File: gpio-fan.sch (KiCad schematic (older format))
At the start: 26 parts, among them J1 Conn_01x05, J2 Conn_01x05, J3 Conn_01x02, J4 Conn_02x07_Odd_Even, J5 Conn_01x03, J6 Conn_01x02, J7 Conn_01x02, J8 Conn_01x02, Q1 BSS214NW, SW1 SW_DIP_x03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

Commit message: Added large via to match 3.8, minor changes
Signed-off-by: Aaron Williams <aaron.w2@gmail.com>
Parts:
- removed J5: Conn_01x03, Connector_Molex:Molex_KK-254_AE-6410-03A_1x03_P2.54mm_Vertical, symbol Connector_Generic:Conn_01x03
- added C9: 1uF, Capacitor_SMD:C_0603_1608Metric, symbol Device:C
- added J5: Conn_01x04_Male, Connector_PinHeader_2.54mm:PinHeader_1x04_P2.54mm_Vertical, symbol Connector:Conn_01x04_Male
- J2: value Conn_01x05 -> Conn_01x05 DNS
- J3: MFR - -> Samtec Inc.; MPN - -> SLM-102-01-S-S; SPN - -> SAM9931-ND; SPR - -> Digikey; SPURL - -> https://www.digikey.com/products/en?mpart=SLM-102-01-S-S&v=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
- J4: MFR - -> Adam Tech; MPN - -> BHR-14-HUA-ML; SPN - -> 2057-BHR-14-HUA-ML-ND; SPR - -> Digikey; SPURL - -> https://www.digikey.com/product-detail/en/adam-tech/BHR-14-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
- J7, J8: value Conn_01x02 -> Conn_01x02 DNS
- R1: value 4.7K -> 1K; DESC (none) -> RES SMD 1K OHM 1% 1/10W 0603; MPN RC0603FR-074K7L -> RC0603FR-071KL; SPN 311-4.70KHRCT-ND -> 311-1.00KHRCT-ND; SPURL https://www.digikey.com/product-detail/en/yageo/RC0603FR-074K7L/311-4.70KHRCT-ND/730159 -> https://www.digikey.com/product-detail/en/yageo/RC0603FR-071KL/311-1.00KHRCT-ND/729790
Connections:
- wire segments 83 -> 89

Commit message: Upgraded to revision 1.3, changed temperature sensor and accelerometer.
This now uses a combined part that should be a lot easier to solder.
The new ST part also includes a temperature sensor and it is supported
by the Arduino library.

Signed-off-by: Aaron Williams <aaron.w2@gmail.com>
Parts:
- removed U2: MXC400XXC, Aaron:MXC400XXC, symbol Aaron:MXC400XXC
- added C10: 0.22uF, Capacitor_SMD:C_0603_1608Metric, symbol Device:C
- added C11: 0.1uF, Capacitor_SMD:C_0603_1608Metric, symbol Device:C
- added C12: 10uF, Capacitor_SMD:C_0603_1608Metric, symbol Device:C
- added U2: LSM303AGRTR, Package_LGA:LGA-12_2x2mm_P0.5mm, symbol Aaron:LSM303AGRTR
- C1, C2, C3, C4, C5, C6, C7, C9, D1, D2, D3, J1, J3, J4, J5, Q1, R2, RN1, SW1, U1: DESC (none) -> -
- C8: value 1uF -> 0.1uF; DESC (none) -> -
- J6: DESC (none) -> -; SPURL https://www.digikey.com/product-detail/en/samtec-inc/SLM-10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 -> https://www.digikey.com/products/en?mpart=SLM-102-01-S-S&v=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
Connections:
- wire segments 89 -> 110
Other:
- moved on the sheet: C8, RN1, SW1

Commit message: Fixed mislabeled capacitor and other minor changes.
Signed-off-by: Aaron Williams <aaron.w2@gmail.com>
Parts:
- added C13: 0.1uF, Capacitor_SMD:C_0603_1608Metric, symbol Device:C
- U1: footprint Aaron:HWQFN-24_EP_4x4_Pitch0.5mm -> Package_DFN_QFN:Texas_S-PVQFN-N24_EP2.1x2.1mm

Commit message: Fixed J6, dimmed LEDs, and added ADC for light sensor
This also expands the board size where the switches are so that it can be
better mounted to the main board via the +5V pins near the speaker connector.

Signed-off-by: Aaron Williams <aaron.w2@gmail.com>
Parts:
- added C14: 1uF, Capacitor_SMD:C_0603_1608Metric, symbol Device:C
- added C15: 0.1uF, Capacitor_SMD:C_0603_1608Metric, symbol Device:C
- added J10: Conn_01x04 DNS, Connector_PinHeader_1.27mm:PinHeader_1x04_P1.27mm_Vertical, symbol Connector:Conn_01x04_Male
- added J9: Conn_01x04 DNS, Connector_PinHeader_2.54mm:PinHeader_1x04_P2.54mm_Vertical, symbol Connector:Conn_01x04_Male
- added R3: 4.7K, Resistor_SMD:R_0603_1608Metric, symbol Device:R
- added U3: ADS1110, Package_TO_SOT_SMD:SOT-23-6, symbol Analog_ADC:ADS1110
- J5: value Conn_01x04_Male -> Conn_01x04 DNS
- R1: value 1K -> 4.7K
- R2: value 33 -> 3.9K; DESC - -> 3.9 kOhms ±1% 0.1W, 1/10W Chip Resistor 0603 (1608 Metric) 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; MFR Yageo -> Bourns Inc.; MPN RC0603FR-0733RL -> CR0603-FX-3901ELF; SPN 311-33.0HRCT-ND -> CR0603-FX-3901ELFCT-ND; SPURL https://www.digikey.com/product-detail/en/yageo/RC0603FR-07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 -> https://www.digikey.com/en/products/detail/bourns-inc/CR060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
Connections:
- net labels added: ADC_IN, PU_OUT
- wire segments 110 -> 130

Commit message: Changed accelerometer due to unavailability
The LSM303AGRTR compass/accelerometer/etc. is out of stock in many places
so this substitutes a LSM6DSL and a LISMDLTR combination instead.

Signed-off-by: Aaron Williams <aaron.w2@gmail.com>
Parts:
- removed U2: LSM303AGRTR, Package_LGA:LGA-12_2x2mm_P0.5mm, symbol Aaron:LSM303AGRTR
- added C16, C17: 0.1uF, Capacitor_SMD:C_0603_1608Metric, symbol Device:C
- added U2: LSM6DSL, Package_LGA:LGA-14_3x2.5mm_P0.5mm_LayoutBorder3x4y, symbol Aaron:LSM6DSL
- added U4: LIS3MDLTR, digikey-footprints:VFLGA-12_2x2mm, symbol dk_Magnetic-Sensors-Linear-Compass-ICs:LIS3MDLTR
- C10: value 0.22uF -> 0.1uF
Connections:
- wire segments 130 -> 147
- no-connect marks 3 -> 4
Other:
- moved on the sheet: C11, C12, C13, C2, C8

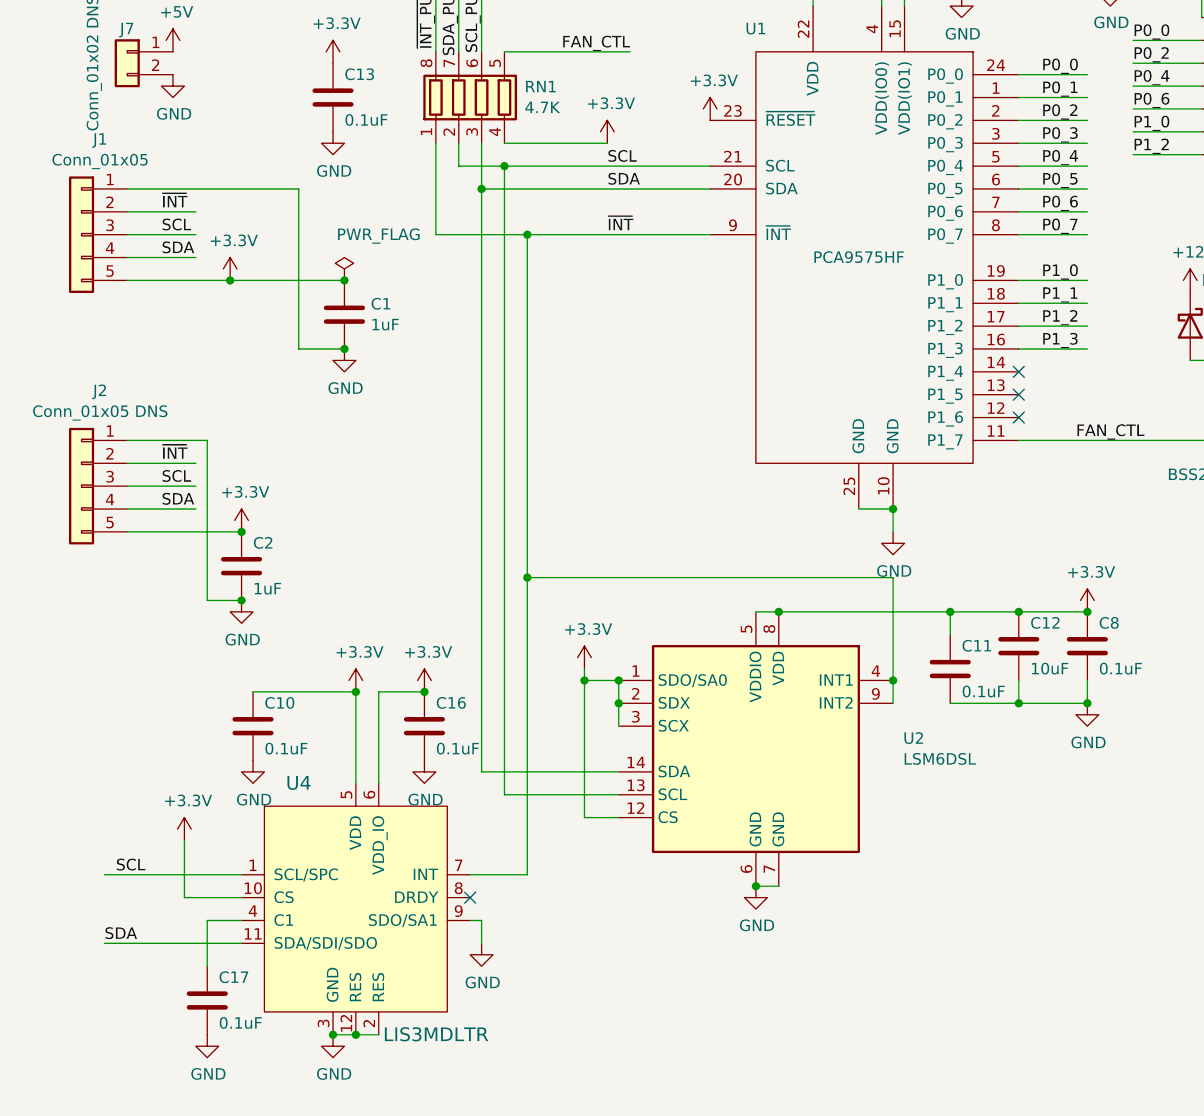
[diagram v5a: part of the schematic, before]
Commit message: Changed sensor to LSM9DS1TR due to availability issues.
Signed-off-by: Aaron Williams <aaron.w2@gmail.com>
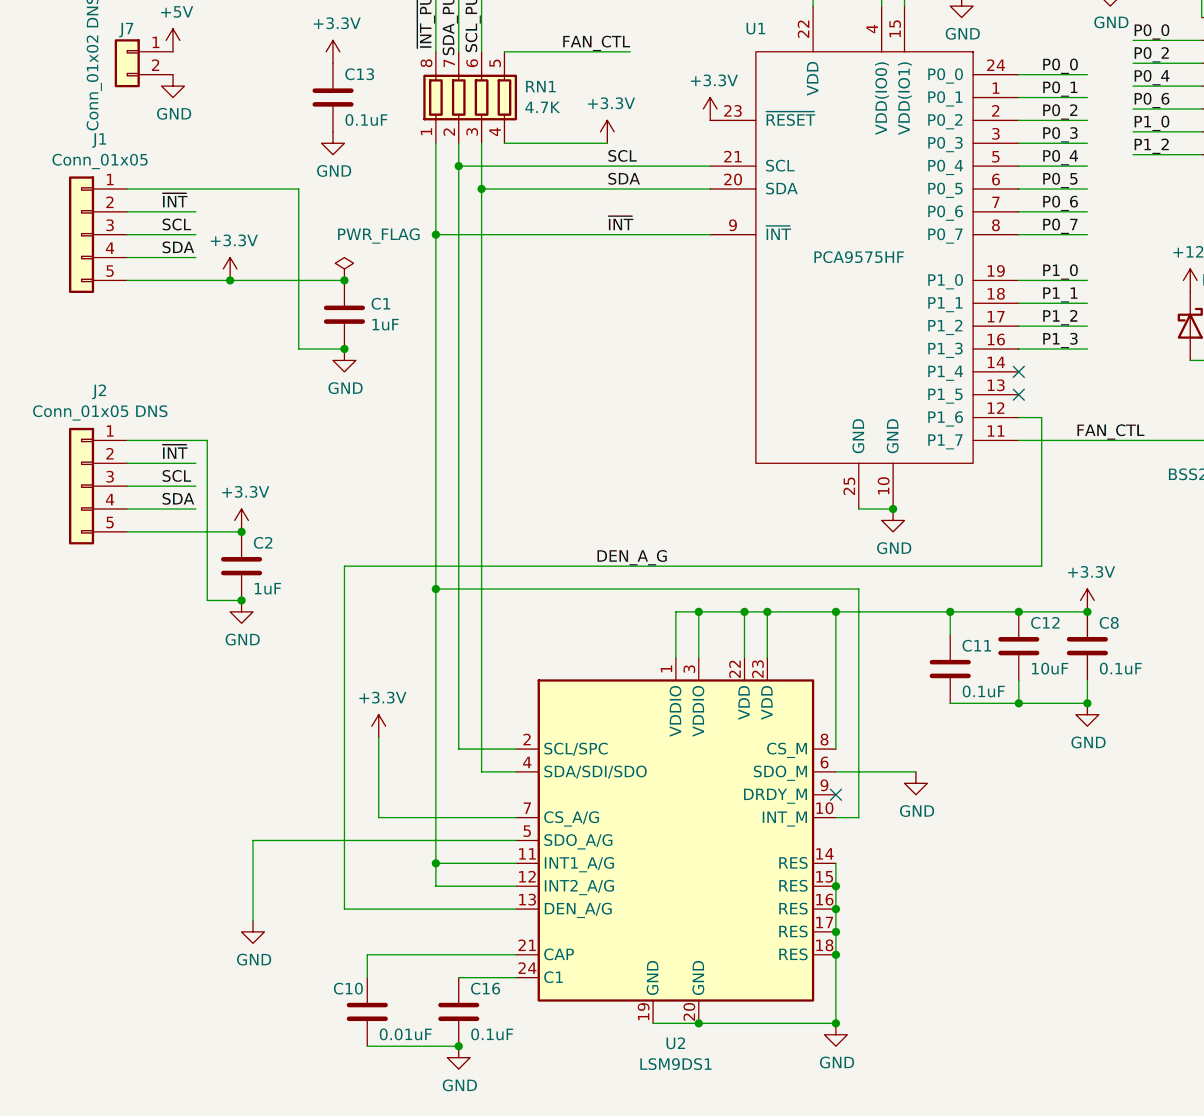
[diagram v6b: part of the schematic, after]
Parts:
- removed C17: 0.1uF, Capacitor_SMD:C_0603_1608Metric, symbol Device:C
- removed U2: LSM6DSL, Package_LGA:LGA-14_3x2.5mm_P0.5mm_LayoutBorder3x4y, symbol Aaron:LSM6DSL
- removed U4: LIS3MDLTR, digikey-footprints:VFLGA-12_2x2mm, symbol dk_Magnetic-Sensors-Linear-Compass-ICs:LIS3MDLTR
- added U2: LSM9DS1, Package_LGA:LGA-24L_3x3.5mm_P0.43mm, symbol Sensor_Motion:LSM9DS1
- C1, C14, C2, C3, C4, C5, C6, C7, C9: MPN CL10B105KA8NNNC -> CL10B105KP8NNNC; SPN 1276-1184-1-ND -> 1276-1946-1-ND
- C10: value 0.1uF -> 0.01uF; DESC - -> 10000pF ±10% 50V Ceramic Capacitor X7R 0603 (1608 Metric); MPN CL10B105KA8NNNC -> CL10B103KB8NCNC; SPN 1276-1184-1-ND -> 1276-1921-1-ND; SPURL - -> https://www.digikey.com/en/products/detail/samsung-electro-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
- C11, C13, C15, C16, C8: MPN CL10B105KA8NNNC -> CL10B104KO8WPNC; SPN 1276-1184-1-ND -> 1276-6582-1-ND
- C12: MFR Samsung -> Murata Electronics; MPN CL10B105KA8NNNC -> GRT188R61E106ME13D; SPN 1276-1184-1-ND -> 490-12323-1-ND
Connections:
- net labels added: DEN_A_G
- wire segments 147 -> 154
- no-connect marks 4 -> 3

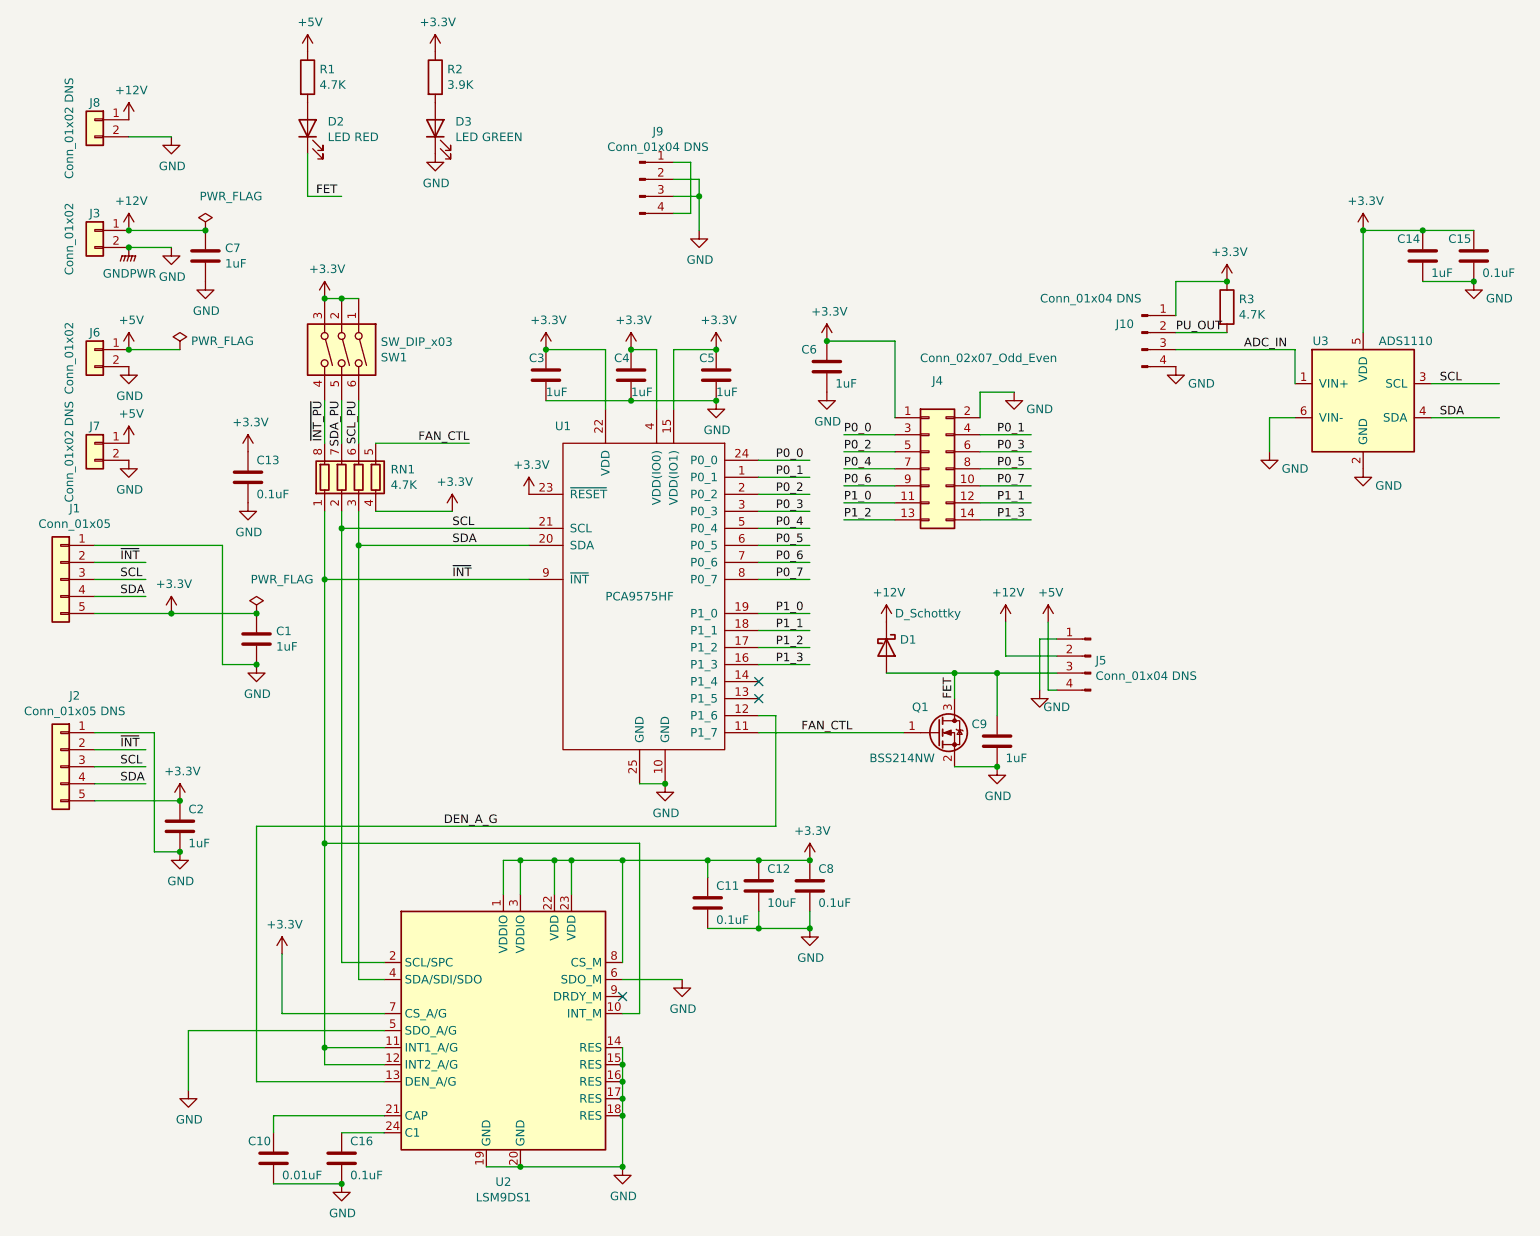
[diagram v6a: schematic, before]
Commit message: V1.9, changed U2 to Bosch BMX180
Signed-off-by: Aaron Williams <aaron.w2@gmail.com>
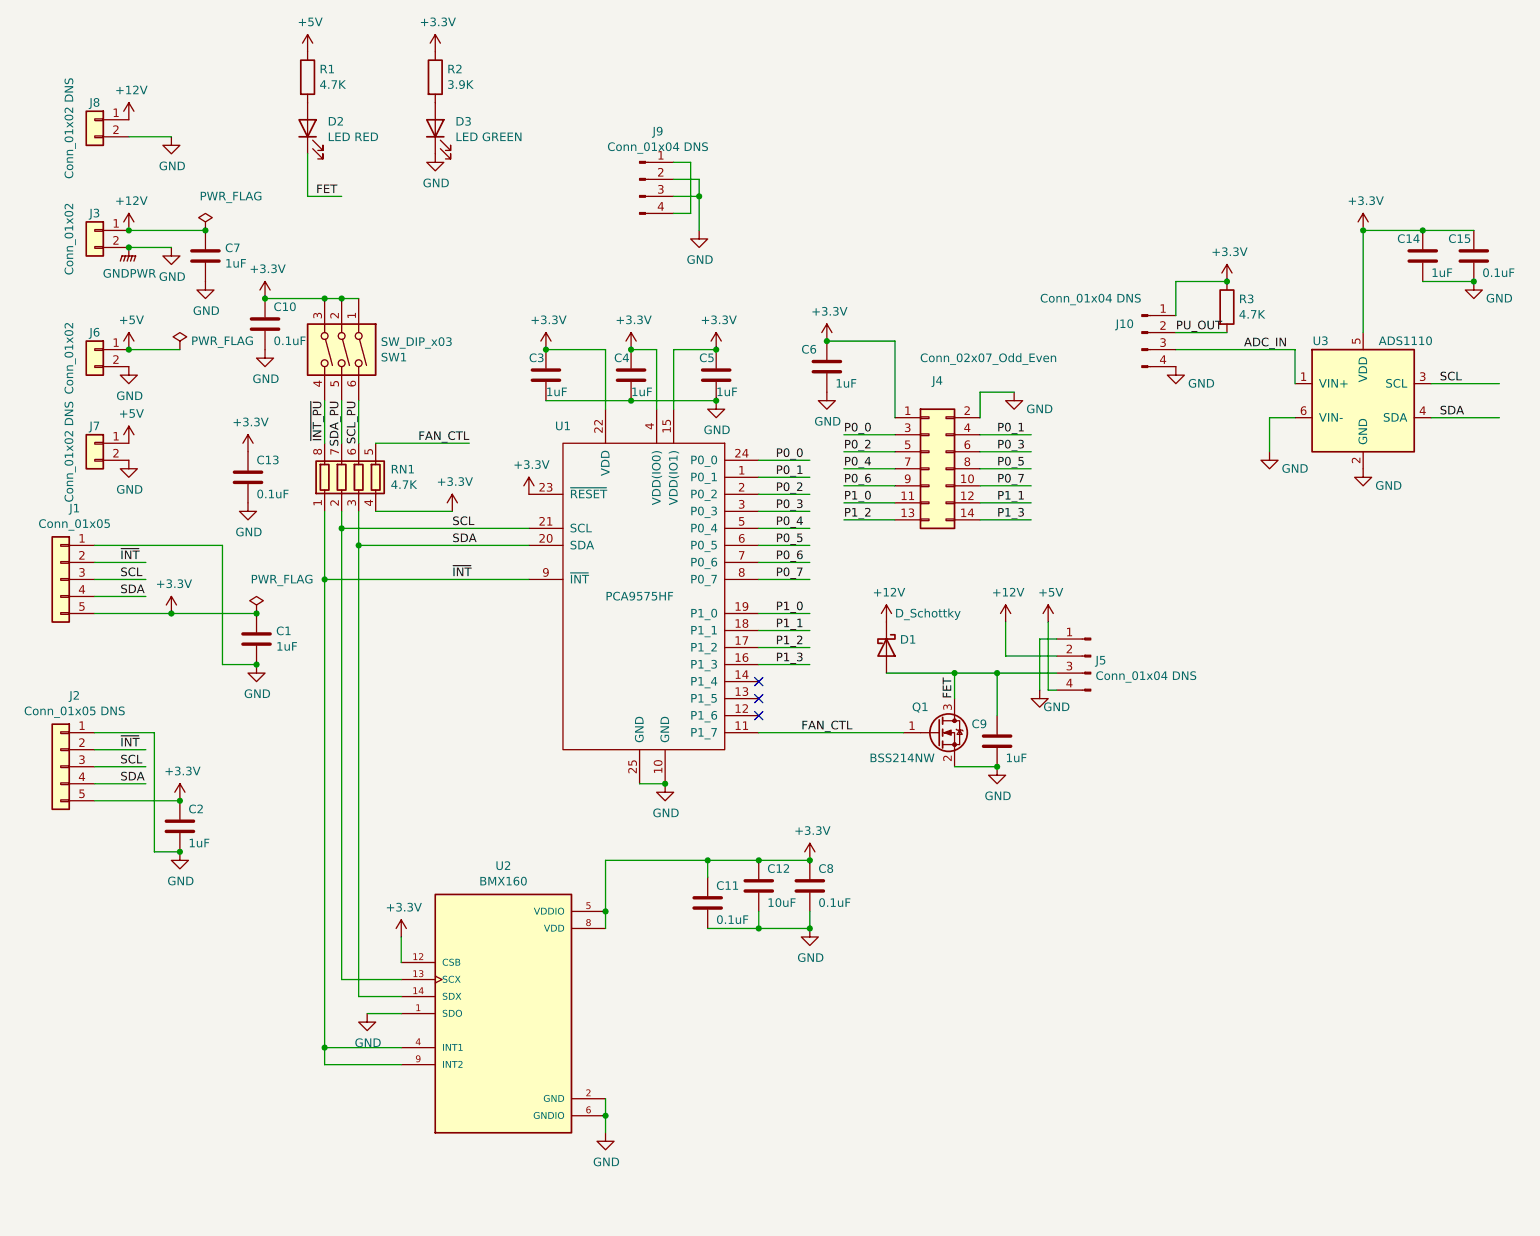
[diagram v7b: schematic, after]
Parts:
- removed C16: 0.1uF, Capacitor_SMD:C_0603_1608Metric, symbol Device:C
- removed U2: LSM9DS1, Package_LGA:LGA-24L_3x3.5mm_P0.43mm, symbol Sensor_Motion:LSM9DS1
- added U2: BMX160, PQFN50P250X300X100-14N, symbol Aaron:BMX160
- C10: value 0.01uF -> 0.1uF; DESC 10000pF ±10% 50V Ceramic Capacitor X7R 0603 (1608 Metric) -> -; MPN CL10B103KB8NCNC -> CL10B104KO8WPNC; SPN 1276-1921-1-ND -> 1276-6582-1-ND; SPURL https://www.digikey.com/en/products/detail/samsung-electro-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 -> -
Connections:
- net labels removed: DEN_A_G
- wire segments 154 -> 127
